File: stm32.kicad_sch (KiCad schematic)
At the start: 47 parts, among them J1 USB_B_Mini, J19 Conn_01x06, J2 Conn_02x05_Odd_Even, J7 TC2030, SW1 SW_Push, SW2 SW_Push, SW3 SW_Push, SW4 SW_Push, U1 STM32F427VGT6, U3 molex_48pin_MRE, U5 LM1117-3.3, X1 8MHz 20pF, Y2 32768 Hz

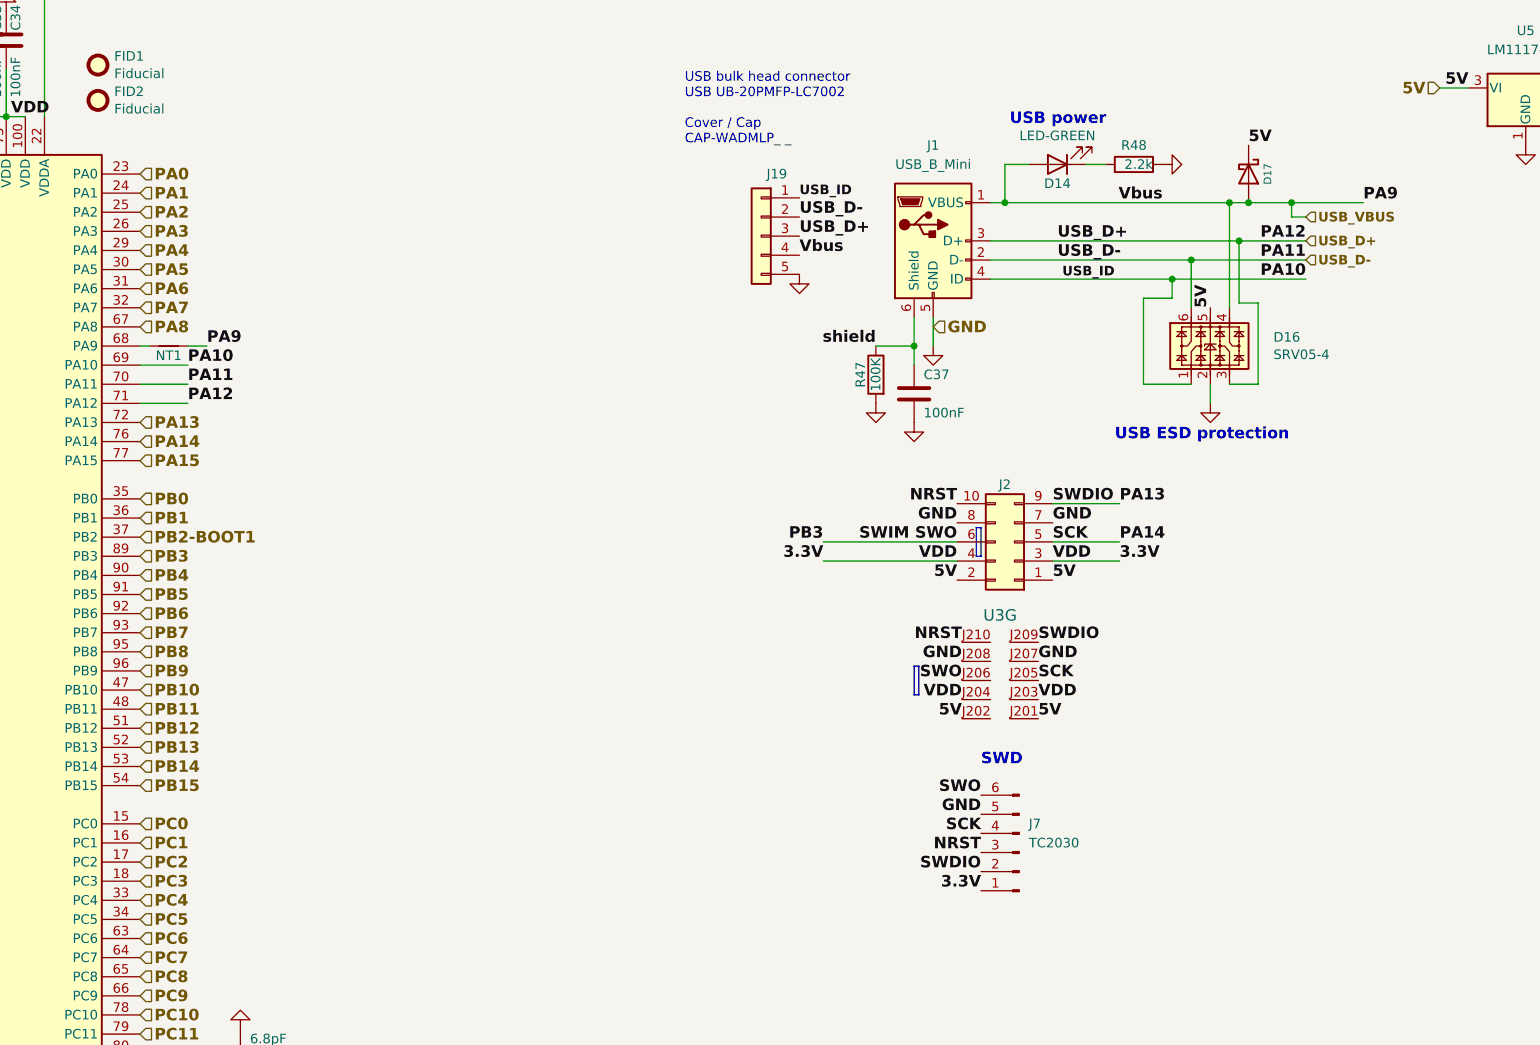
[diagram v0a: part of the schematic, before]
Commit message: replaces micro b connector by usb-c
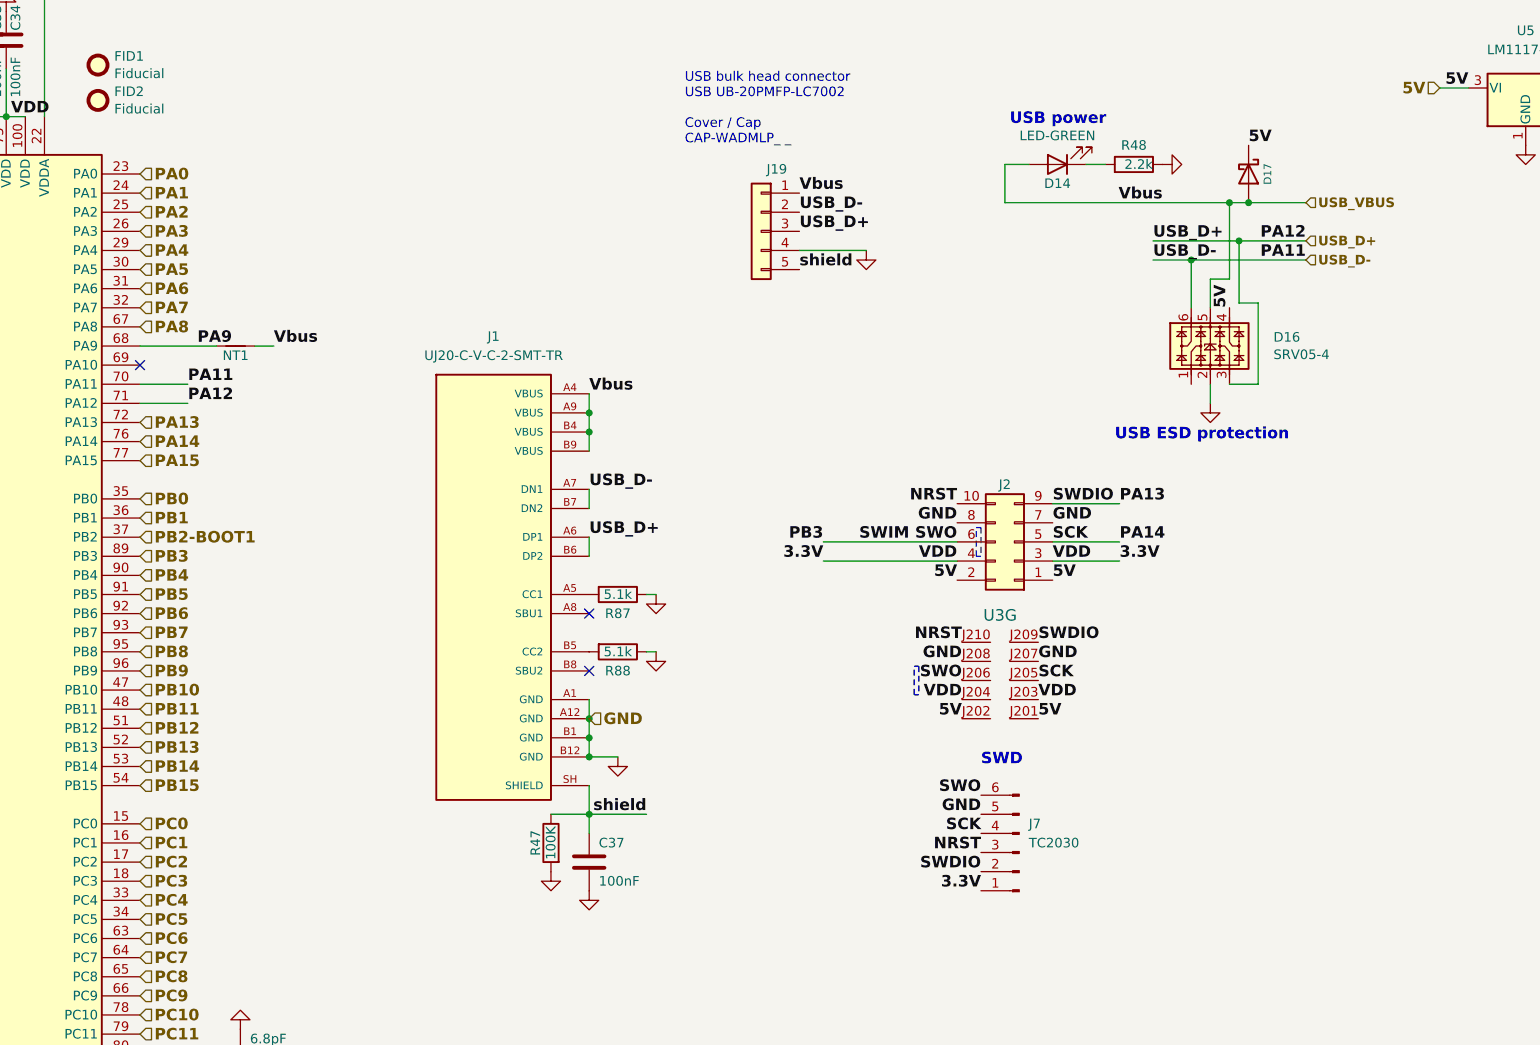
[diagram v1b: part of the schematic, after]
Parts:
- removed J1: USB_B_Mini, hellen-one-common:USB-MINI-B-VERTICAL, symbol hellen-one-common:USB_B_Mini
- added J1: UJ20-C-V-C-2-SMT-TR, UJ20_C_V_C_2_SMT_TR:CUI_UJ20-C-V-C-2-SMT-TR, symbol UJ20-C-V-C-2-SMT-TR:UJ20-C-V-C-2-SMT-TR
- added R87, R88: 5.1k, Resistor_SMD:R_0603_1608Metric, symbol Device:R
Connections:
- net 5V: now also D16.4; no longer D16.5
- net GND: now also J19.4 (Pin_4), J1.A1 (GND), J1.A12 (GND), J1.B1 (GND), J1.B12 (GND), R87.1, R88.1; no longer J19.5 (Pin_5)
- net USB_D+: now also J1.A6 (DP1), J1.B6 (DP2)
- net USB_D-: now also J1.A7 (DN1), J1.B7 (DN2)
- net USB_VBUS: now also D16.5, J19.1 (Pin_1), J1.A4 (VBUS), J1.A9 (VBUS), J1.B4 (VBUS), J1.B9 (VBUS); no longer D16.4, J19.4 (Pin_4)
- net shield: now also J19.5 (Pin_5), J1.SH (SHIELD)
- net PA9: now reaches NT1.1, U1.68 (PA9)
- removed net PA10: D16.1, J19.1 (Pin_1), U1.69 (PA10)
- new net: J1.B5 (CC2), R88.2
- new net: J1.A5 (CC1), R87.2
- no-connect marks 0 -> 3
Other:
- moved on the sheet: C37, J19, NT1, R47

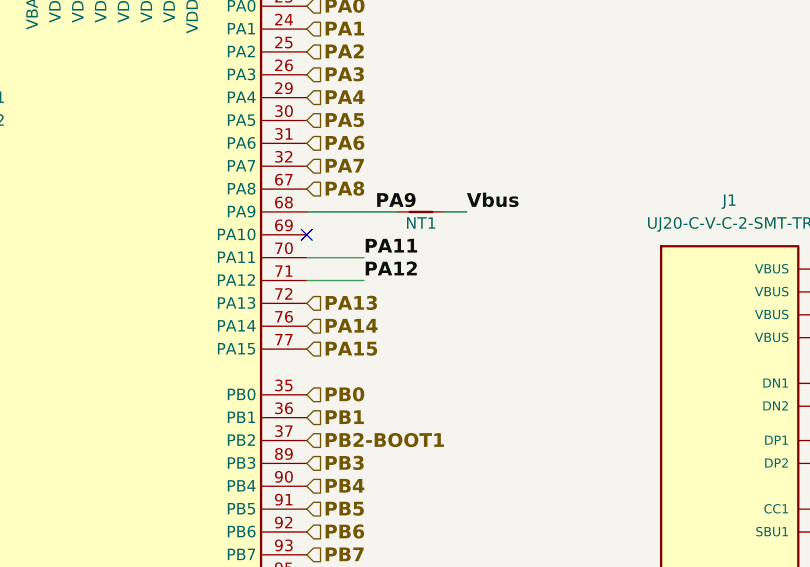
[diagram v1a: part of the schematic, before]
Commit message: widened usb trace to further reduce impedence
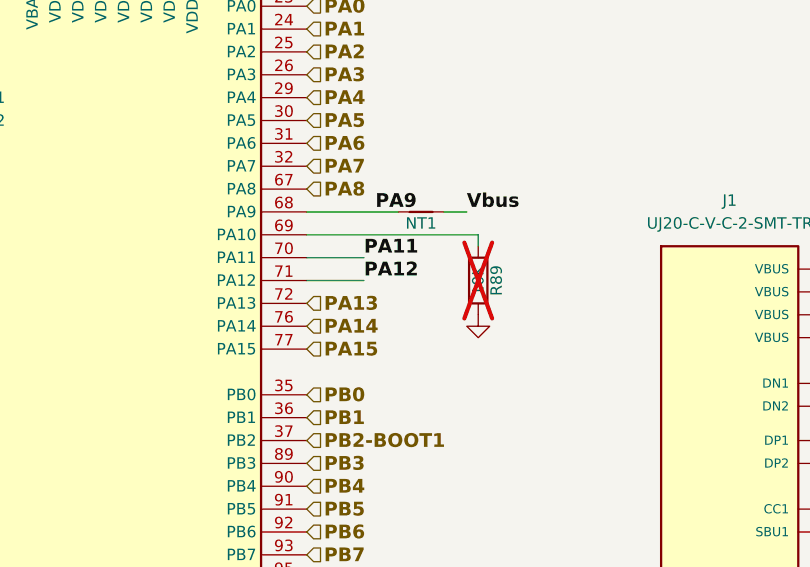
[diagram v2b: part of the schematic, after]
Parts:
- added R89: 10K, Resistor_SMD:R_0603_1608Metric, symbol Device:R
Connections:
- net GND: now also R89.1
- net at U1.69 (PA10): now also R89.2
- no-connect marks 3 -> 2
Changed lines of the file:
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@@
 	)
 	(no_connect
-		(at 186.69 123.19)
-	)
-	(no_connect
 		(at 246.38 163.83)
 	)
@@
 	(wire
 		(pts
+			(xy 205.74 123.19) (xy 205.74 124.46)
+		)
+		(stroke
+			(width 0)
+			(type default)
+		)
+	)
+	(wire
+		(pts
 			(xy 246.38 179.07) (xy 246.38 182.88)
 		)
@@
 	(wire
 		(pts
+			(xy 186.69 123.19) (xy 205.74 123.19)
+		)
+		(stroke
+			(width 0)
+			(type default)
+		)
+	)
+	(wire
+		(pts
 			(xy 386.08 80.645) (xy 386.08 86.36)
 		)
@@
 	)
 	(symbol
+		(lib_id "Device:R")
+		(at 205.74 128.27 0)
+		(mirror x)
+		(unit 1)
+		(exclude_from_sim no)
+		(in_bom yes)
+		(on_board yes)
+		(dnp yes)
+		(property "Reference" "R89"
+			(at 207.772 128.27 90)
+			(effects
+				(font
+					(size 1.27 1.27)
+				)
+			)
+		)
+		(property "Value" "10K"
+			(at 205.74 128.27 90)
+			(effects
+				(font
+					(size 1.27 1.27)
+				)
+			)
+		)
+		(property "Footprint" "Resistor_SMD:R_0603_1608Metric"
+			(at 264.922 186.69 90)
+			(effects
+				(font
+					(size 1.524 1.524)
+				)
+				(hide yes)
+			)
+		)
+		(property "Datasheet" "TBD"
+			(at 354.33 187.325 0)
+			(effects
+				(font
+					(size 1.524 1.524)
+				)
+				(hide yes)
+			)
+		)
+		(property "Description" ""
+			(at 205.74 128.27 0)
+			(effects
+				(font
+					(size 1.27 1.27)
+				)
+			)
+		)
+		(property "Part #" "RMCF0603JT10K0"
+			(at 87.63 21.59 0)
+			(effects
+				(font
+					(size 1.27 1.27)
+				)
+				(hide yes)
+			)
+		)
+		(property "VEND" "DIGI"
+			(at 87.63 21.59 0)
+			(effects
+				(font
+					(size 1.27 1.27)
+				)
+				(hide yes)
+			)
+		)
+		(property "VEND#" "RMCF0603JT10K0CT-ND"
+			(at 87.63 21.59 0)
+			(effects
+				(font
+					(size 1.27 1.27)
+				)
+				(hide yes)
+			)
+		)
+		(property "Manufacturer" "StackPole"
+			(at 87.63 21.59 0)
+			(effects
+				(font
+					(size 1.27 1.27)
+				)
+				(hide yes)
+			)
+		)
+		(property "LCSC" "C25804"
+			(at 205.74 128.27 0)
+			(effects
+				(font
+					(size 1.27 1.27)
+				)
+				(hide yes)
+			)
+		)
+		(pin "1"
+		)
+		(pin "2"
+		)
+		(instances
+			(project "micro_rusEFI"
+				(path "/8d063f79-9282-4820-bcf4-1ff3c006cf08/00000000-0000-0000-0000-00005d0250fb"
+					(reference "R89")
+					(unit 1)
+				)
+			)
+		)
+	)
+	(symbol
 		(lib_id "UJ20-C-V-C-2-SMT-TR:UJ20-C-V-C-2-SMT-TR")
 		(at 233.68 147.32 0)
@@
 					(unit 1)
 				)
+			)
+		)
+	)
+	(symbol
+		(lib_id "power:GND")
+		(at 205.74 132.08 0)
+		(unit 1)
+		(exclude_from_sim no)
+		(in_bom yes)
+		(on_board yes)
+		(dnp no)
+		(property "Reference" "#PWR0126"
+			(at 205.74 132.08 0)
+			(effects
+				(font
+					(size 0.762 0.762)
+				)
+				(hide yes)
+			)
+		)
+		(property "Value" "GND"
+			(at 205.74 133.858 0)
+			(effects
+				(font
+					(size 0.762 0.762)
+				)
+				(hide yes)
+			)
+		)
+		(property "Footprint" ""
+			(at 205.74 132.08 0)
+			(effects
+				(font
+					(size 1.524 1.524)
+				)
+			)
+		)
+		(property "Datasheet" ""
+			(at 205.74 132.08 0)
+			(effects
+				(font
+					(size 1.524 1.524)
+				)
+			)
+		)
+		(property "Description" ""
+			(at 205.74 132.08 0)
+			(effects
+				(font
+					(size 1.27 1.27)
+				)
+			)
+		)
+		(pin "1"
+		)
+		(instances
+			(project "micro_rusEFI"
+				(path "/8d063f79-9282-4820-bcf4-1ff3c006cf08/00000000-0000-0000-0000-00005d0250fb"
+					(reference "#PWR0126")
+					(unit 1)
+				)

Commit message: completed board, created BOM
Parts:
- C39: footprint Capacitor_SMD:C_0603_1608Metric -> Capacitor_SMD:C_0805_2012Metric
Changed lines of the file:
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@@
 			)
 		)
-		(property "Footprint" "Capacitor_SMD:C_0603_1608Metric"
+		(property "Footprint" "Capacitor_SMD:C_0805_2012Metric"
 			(at 303.022 40.64 90)
 			(effects
